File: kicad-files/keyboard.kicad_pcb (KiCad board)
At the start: 2 copper layers, 361.7 x 100 mm, 189 parts, among them J1 TYPE-C-31-M12_13, Q1 2N7002, Q2 2N7002, SW1 K2-1187SQ-A4SW-06, T1 53261-0471, T2 53261-0471, U1 STM32F411CEU6, U2 USBLC6-2SC6, U3 AT24C256C-SSHL-T, U4 SGM2007-3.3XN5/TR, Y1 TAXM8M4RFDCET2T

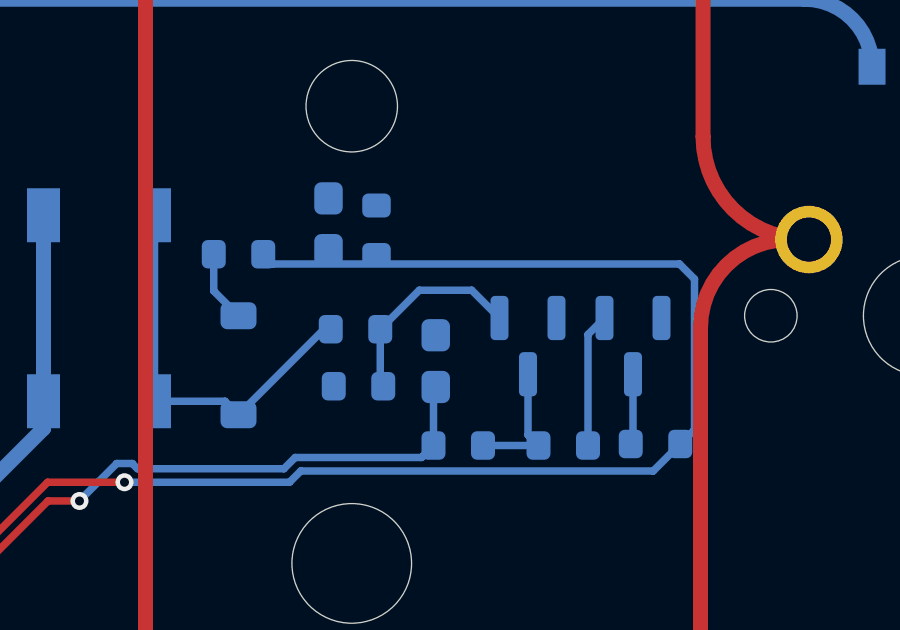
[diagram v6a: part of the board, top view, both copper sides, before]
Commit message: Moved some devices further away from stab mount
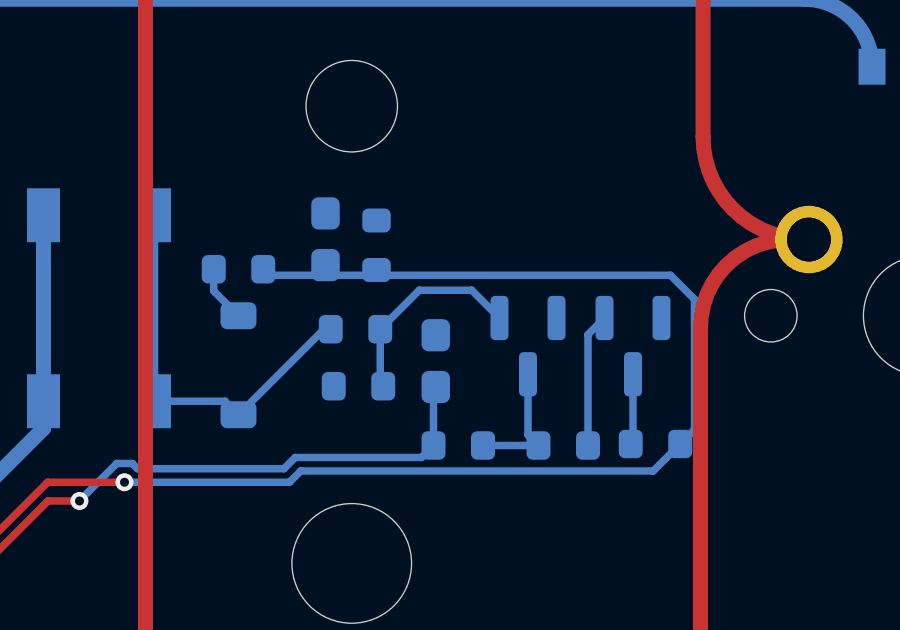
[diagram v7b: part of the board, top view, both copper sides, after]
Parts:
- moved C8 0.51 mm to (295.0, 47.6)
- moved R13 0.50 mm to (292.1, 48.6)
- moved R14 0.50 mm to (296.7, 47.8)
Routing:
- net Net-(U1-BOOT0): track 55.0 -> 54.4 mm
- net Net-(D_72-K): track 2.39 -> 1.89 mm
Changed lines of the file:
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@@
   )
   (footprint "Resistor_SMD:R_0603_1608Metric" (layer "B.Cu")
-    (at 296.7 47.3 90)
+    (at 296.7 47.8 90)
     (descr "Resistor SMD 0603 (1608 Metric), square (rectangular) end terminal, IPC_7351 nominal, (Body size source: IPC-SM-782 page 72, https://www.pcb-3d.com/wordpress/wp-content/uploads/ipc-sm-782a_amendment_1_and_2.pdf), generated with kicad-footprint-generator")
     (tags "resistor")
@@
   )
   (footprint "Capacitor_SMD:C_0603_1608Metric_Pad1.08x0.95mm_HandSolder" (layer "B.Cu")
-    (at 295.1 47.1 90)
+    (at 295 47.6 90)
     (descr "Capacitor SMD 0603 (1608 Metric), square (rectangular) end terminal, IPC_7351 nominal with elongated pad for handsoldering. (Body size source: IPC-SM-782 page 76, https://www.pcb-3d.com/wordpress/wp-content/uploads/ipc-sm-782a_amendment_1_and_2.pdf), generated with kicad-footprint-generator")
     (tags "capacitor handsolder")
@@
     (property "ki_keywords" "cap capacitor")
     (attr smd)
-    (fp_text reference "C8" (at 1.8 0 180) (layer "B.SilkS")
+    (fp_text reference "C8" (at 1.9 0.2 180) (layer "B.SilkS")
         (effects (font (size 1 1) (thickness 0.15)) (justify mirror))
     )
@@
   )
   (footprint "Resistor_SMD:R_0603_1608Metric" (layer "B.Cu")
-    (at 292.1 48.1 180)
+    (at 292.1 48.6 180)
     (descr "Resistor SMD 0603 (1608 Metric), square (rectangular) end terminal, IPC_7351 nominal, (Body size source: IPC-SM-782 page 72, https://www.pcb-3d.com/wordpress/wp-content/uploads/ipc-sm-782a_amendment_1_and_2.pdf), generated with kicad-footprint-generator")
     (tags "resistor")
@@
     (property "ki_keywords" "R res resistor")
     (attr smd)
-    (fp_text reference "R10" (at 0.3 3.1) (layer "B.SilkS")
+    (fp_text reference "R10" (at 0.3 2.9) (layer "B.SilkS")
         (effects (font (size 1 1) (thickness 0.15)) (justify mirror))
     )
@@
   (via (at 288.3 55.7) (size 0.6) (drill 0.3) (layers "F.Cu" "B.Cu") (net 116))
   (via (at 277.622461 63.814063) (size 0.6) (drill 0.3) (layers "F.Cu" "B.Cu") (net 116))
-  (segment (start 307.3 48.925) (end 306.8 48.425) (width 0.25) (layer "B.Cu") (net 116))
+  (segment (start 292.925 48.6) (end 293.125 48.8) (width 0.25) (layer "B.Cu") (net 116))
   (segment (start 288.3 55.7) (end 293.8 55.7) (width 0.25) (layer "B.Cu") (net 116))
   (segment (start 305.925 55.325) (end 306.825 54.425) (width 0.25) (layer "B.Cu") (net 116))
-  (segment (start 307.3 53.95) (end 307.3 48.925) (width 0.25) (layer "B.Cu") (net 116))
   (segment (start 293.8 55.7) (end 294.175 55.325) (width 0.25) (layer "B.Cu") (net 116))
+  (segment (start 306.5 48.8) (end 307.3 49.6) (width 0.25) (layer "B.Cu") (net 116))
+  (segment (start 307.3 53.95) (end 306.825 54.425) (width 0.25) (layer "B.Cu") (net 116))
   (segment (start 294.175 55.325) (end 305.925 55.325) (width 0.25) (layer "B.Cu") (net 116))
-  (segment (start 306.8 48.425) (end 293.25 48.425) (width 0.25) (layer "B.Cu") (net 116))
-  (segment (start 306.825 54.425) (end 307.3 53.95) (width 0.25) (layer "B.Cu") (net 116))
-  (segment (start 293.25 48.425) (end 292.925 48.1) (width 0.25) (layer "B.Cu") (net 116))
+  (segment (start 293.125 48.8) (end 306.5 48.8) (width 0.25) (layer "B.Cu") (net 116))
+  (segment (start 307.3 49.6) (end 307.3 53.95) (width 0.25) (layer "B.Cu") (net 116))
   (segment (start 277.604919 65.166315) (end 277.604919 63.645081) (width 0.25) (layer "B.Cu") (net 116))
   (segment (start 306.170725 17.770725) (end 313.268399 17.770725) (width 0.5) (layer "B.Cu") (net 117))
@@
   (arc (start 301.7 93.1) (mid 303.609188 92.309188) (end 304.4 90.4) (width 0.5) (layer "B.Cu") (net 121))
   (arc (start 244.55 93.1) (mid 246.459188 92.309188) (end 247.25 90.4) (width 0.5) (layer "B.Cu") (net 121))
+  (segment (start 291.275 48.6) (end 291.275 49.325) (width 0.25) (layer "B.Cu") (net 122))
   (segment (start 291.275 49.325) (end 292.1 50.15) (width 0.25) (layer "B.Cu") (net 122))
-  (segment (start 291.275 48.1) (end 291.275 49.325) (width 0.25) (layer "B.Cu") (net 122))
   (segment (start 294.95 50.6) (end 292.1 53.45) (width 0.25) (layer "B.Cu") (net 123))
   (segment (start 289.3 46.8) (end 289.3 53) (width 0.25) (layer "B.Cu") (net 123))

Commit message: Added cut-outs around arrow keys and fixed boarder size
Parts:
- moved D_68 0.65 mm to (246.6, 88.8)
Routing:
- net R4: track 280.9 -> 342.8 mm
- net R3: track 324.0 -> 320.1 mm
- net C16: track 88.5 -> 91.6 mm
- net Net-(D_68-A): track 8.07 -> 7.42 mm
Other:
- board size 361.7 x 100 mm -> 362 x 100 mm
